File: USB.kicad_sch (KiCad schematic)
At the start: 13 parts, among them J2 USB_B, U1 FT232RL, U2 ADuM121N

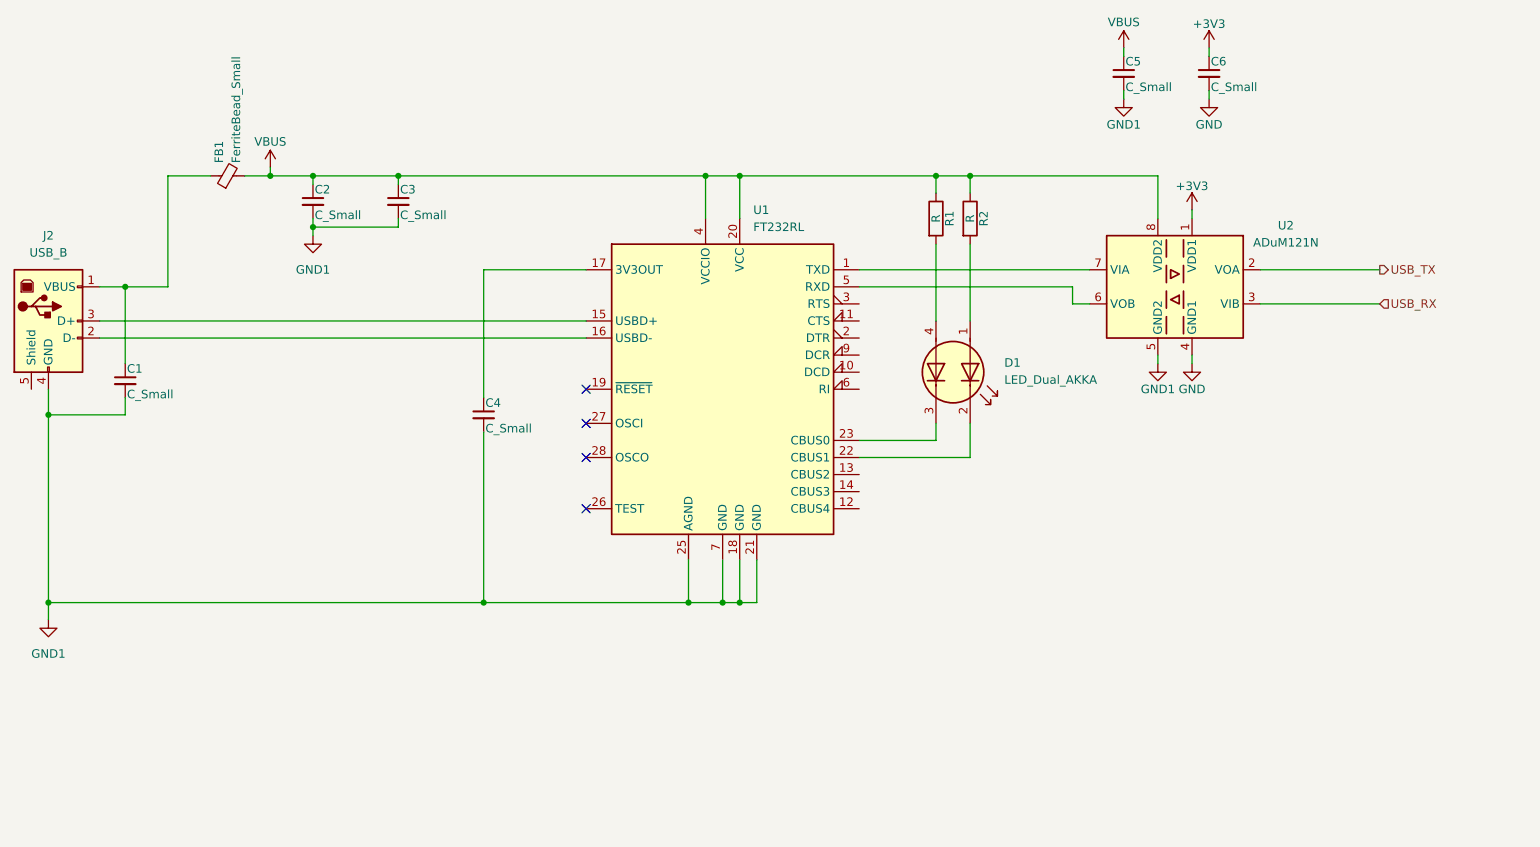
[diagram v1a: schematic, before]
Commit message: analog inputs, timer IO
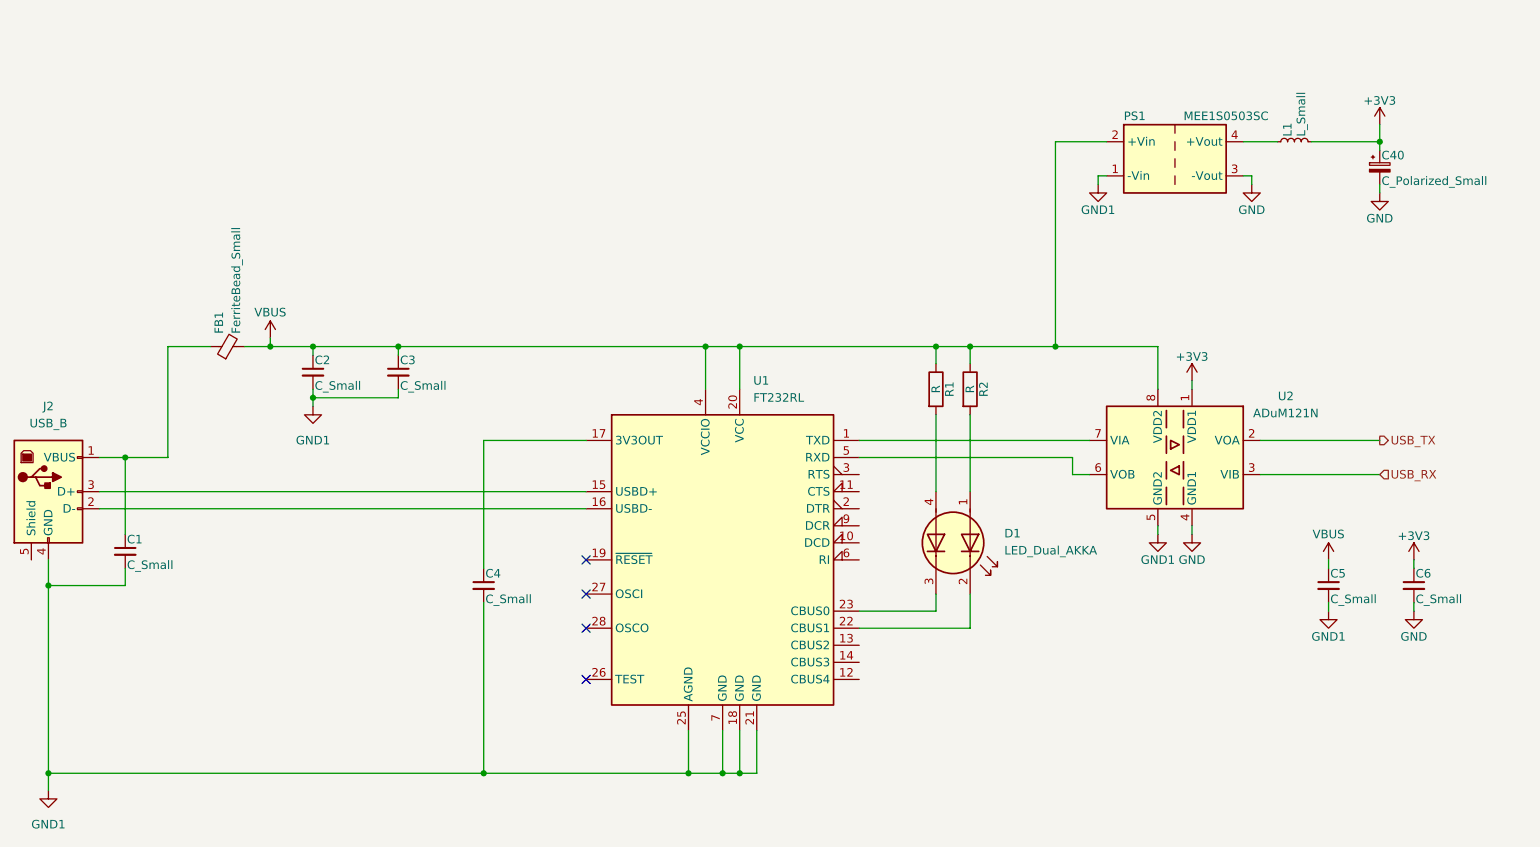
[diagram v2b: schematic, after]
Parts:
- added C40: C_Polarized_Small, symbol Device:C_Polarized_Small
- added L1: L_Small, symbol Device:L_Small
- added PS1: MEE1S0503SC, Converter_DCDC:Converter_DCDC_Murata_MEE1SxxxxSC_THT, symbol Converter_DCDC:MEE1S0503SC
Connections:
- net +3V3: now also C40.1, L1.2
- net GND: now also C40.2, PS1.3 (-Vout)
- net GND1: now also PS1.1 (-Vin)
- net VBUS: now also PS1.2 (+Vin)
- new net: L1.1, PS1.4 (+Vout)
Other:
- moved on the sheet: C1, C2, C3, C4, C5, C6, D1, FB1, J2, R1, R2, U1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

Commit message: first draft schematic?
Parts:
- C1, C2, C3, C4, C5, C6: footprint (none) -> Capacitor_SMD:C_0603_1608Metric
- C40: value C_Polarized_Small -> CE_10uF_16V; footprint (none) -> Capacitor_SMD:CP_Elec_4x5.3; Capacitance (none) -> 10uF; MPN (none) -> MCESL16V106M4X5.2; Voltage (none) -> 16V
- FB1: footprint (none) -> Inductor_SMD:L_0603_1608Metric
- L1: value L_Small -> L_4.7uH_800mA_82472C; footprint (none) -> Inductor_SMD:L_0603_1608Metric; Inductance (none) -> 4.7uH
- R1, R2: footprint (none) -> Resistor_SMD:R_0603_1608Metric
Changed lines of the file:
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@@
     (property "Reference" "R1" (id 0) (at 177.292 72.39 90))
     (property "Value" "R" (id 1) (at 175.26 72.39 90))
-    (property "Footprint" "" (id 2) (at 173.482 72.39 90)
+    (property "Footprint" "Resistor_SMD:R_0603_1608Metric" (id 2) (at 173.482 72.39 90)
       (effects (font (size 1.27 1.27)) hide)
     )
@@
       (effects (font (size 1.27 1.27)) (justify left))
     )
-    (property "Footprint" "" (id 2) (at 95.25 69.85 0)
+    (property "Footprint" "Capacitor_SMD:C_0603_1608Metric" (id 2) (at 95.25 69.85 0)
       (effects (font (size 1.27 1.27)) hide)
     )
@@
       (effects (font (size 1.27 1.27)) (justify left))
     )
-    (property "Footprint" "" (id 2) (at 82.55 69.85 0)
+    (property "Footprint" "Capacitor_SMD:C_0603_1608Metric" (id 2) (at 82.55 69.85 0)
       (effects (font (size 1.27 1.27)) hide)
     )
@@
       (effects (font (size 1.27 1.27)) (justify left))
     )
-    (property "Footprint" "" (id 2) (at 246.38 101.6 0)
+    (property "Footprint" "Capacitor_SMD:C_0603_1608Metric" (id 2) (at 246.38 101.6 0)
       (effects (font (size 1.27 1.27)) hide)
     )
@@
       (effects (font (size 1.27 1.27)) (justify left))
     )
-    (property "Footprint" "" (id 2) (at 233.68 101.6 0)
+    (property "Footprint" "Capacitor_SMD:C_0603_1608Metric" (id 2) (at 233.68 101.6 0)
       (effects (font (size 1.27 1.27)) hide)
     )
@@
     (property "Reference" "R2" (id 0) (at 182.372 72.39 90))
     (property "Value" "R" (id 1) (at 180.34 72.39 90))
-    (property "Footprint" "" (id 2) (at 178.562 72.39 90)
+    (property "Footprint" "Resistor_SMD:R_0603_1608Metric" (id 2) (at 178.562 72.39 90)
       (effects (font (size 1.27 1.27)) hide)
     )
@@
       (effects (font (size 1.27 1.27)) (justify left))
     )
-    (property "Footprint" "" (id 2) (at 69.85 67.818 90)
+    (property "Footprint" "Inductor_SMD:L_0603_1608Metric" (id 2) (at 69.85 67.818 90)
       (effects (font (size 1.27 1.27)) hide)
     )
@@
   (symbol (lib_id "Device:L_Small") (at 228.6 35.56 90) (unit 1)
     (in_bom yes) (on_board yes)
-    (property "Reference" "L1" (id 0) (at 227.584 34.798 0)
-      (effects (font (size 1.27 1.27)) (justify left))
-    )
-    (property "Value" "L_Small" (id 1) (at 229.616 34.798 0)
-      (effects (font (size 1.27 1.27)) (justify left))
-    )
-    (property "Footprint" "" (id 2) (at 228.6 35.56 0)
+    (property "Reference" "L1" (id 0) (at 229.87 33.02 90)
+      (effects (font (size 1.27 1.27)) (justify left))
+    )
+    (property "Value" "L_4.7uH_800mA_82472C" (id 1) (at 229.616 34.798 0)
+      (effects (font (size 1.27 1.27)) (justify left) hide)
+    )
+    (property "Footprint" "Inductor_SMD:L_0603_1608Metric" (id 2) (at 228.6 35.56 0)
       (effects (font (size 1.27 1.27)) hide)
     )
     (property "Datasheet" "~" (id 3) (at 228.6 35.56 0)
       (effects (font (size 1.27 1.27)) hide)
+    )
+    (property "Inductance" "4.7uH" (id 4) (at 228.6 36.83 90)
+      (effects (font (size 1 1)))
     )
     (pin "1")
@@
       (effects (font (size 1.27 1.27)) (justify left))
     )
-    (property "Footprint" "" (id 2) (at 54.61 96.52 0)
+    (property "Footprint" "Capacitor_SMD:C_0603_1608Metric" (id 2) (at 54.61 96.52 0)
       (effects (font (size 1.27 1.27)) hide)
     )
@@
       (effects (font (size 1.27 1.27)) (justify left))
     )
-    (property "Value" "C_Polarized_Small" (id 1) (at 241.554 41.402 0)
-      (effects (font (size 1.27 1.27)) (justify left))
-    )
-    (property "Footprint" "" (id 2) (at 241.3 39.37 0)
-      (effects (font (size 1.27 1.27)) hide)
-    )
-    (property "Datasheet" "~" (id 3) (at 241.3 39.37 0)
-      (effects (font (size 1.27 1.27)) hide)
+    (property "Value" "CE_10uF_16V" (id 1) (at 241.554 41.402 0)
+      (effects (font (size 1.27 1.27)) (justify left) hide)
+    )
+    (property "Footprint" "Capacitor_SMD:CP_Elec_4x5.3" (id 2) (at 241.3 39.37 0)
+      (effects (font (size 1.27 1.27)) hide)
+    )
+    (property "Datasheet" "https://www.farnell.com/datasheets/2883297.pdf" (id 3) (at 241.3 39.37 0)
+      (effects (font (size 1.27 1.27)) hide)
+    )
+    (property "MPN" "MCESL16V106M4X5.2" (id 4) (at 241.3 39.37 0)
+      (effects (font (size 1.27 1.27)) hide)
+    )
+    (property "Capacitance" "10uF" (id 5) (at 241.935 41.275 0)
+      (effects (font (size 1 1)) (justify left))
+    )
+    (property "Voltage" "16V" (id 6) (at 241.935 43.18 0)
+      (effects (font (size 1 1)) (justify left))
     )
     (pin "1")
@@
       (effects (font (size 1.27 1.27)) (justify left))
     )
-    (property "Footprint" "" (id 2) (at 107.95 101.6 0)
-      (effects (font (size 1.27 1.27)) hide)
-    )
+    (property "Footprint" "Capacitor_SMD:C_0603_1608Metric" (id 2) (at 107.95 101.6 0)
+      (effects (font (size 1.27 1.27)) hide)
+    )
